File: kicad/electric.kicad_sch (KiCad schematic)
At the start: 11 parts, among them U1 NodeMCU1.0(ESP-12E), U2 LM7805_TO220

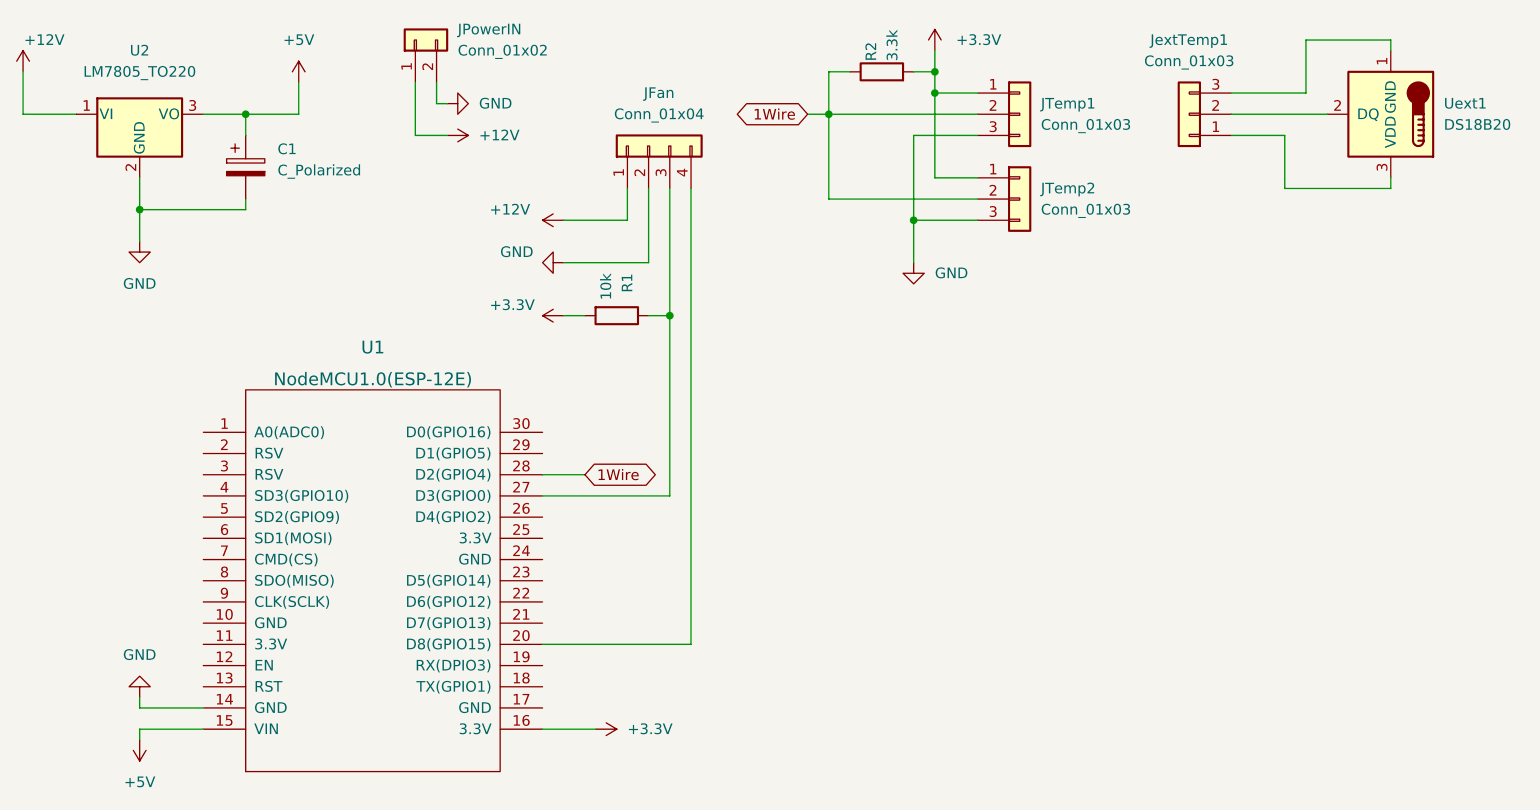
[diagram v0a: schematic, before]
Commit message: feat(kicad): added inverted pwm with npn transistor
Signed-off-by: Mario-F <github@fritschen.net>
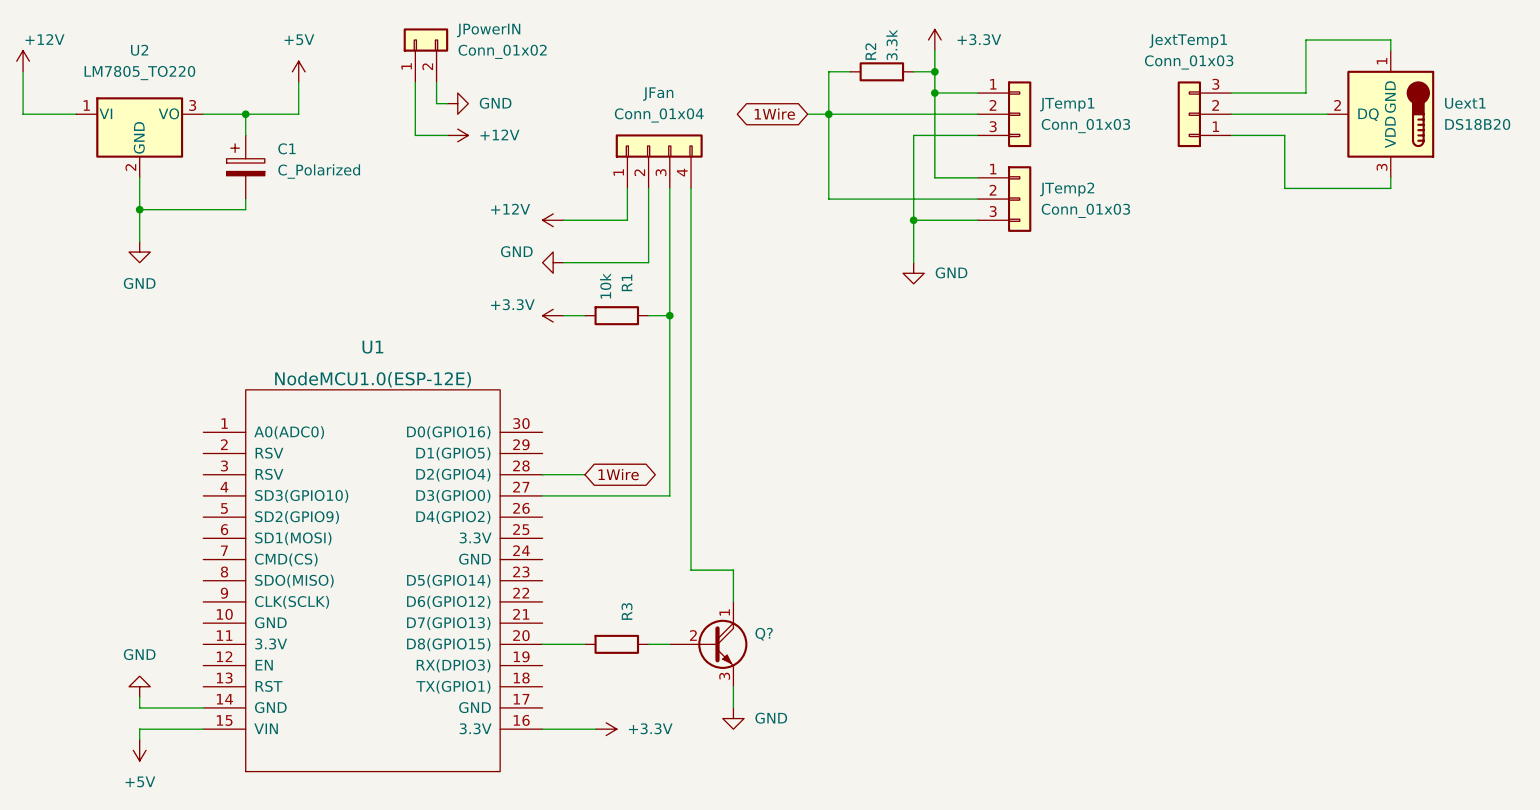
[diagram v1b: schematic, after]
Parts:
- added Q?: (no value), symbol Transistor_BJT:BC517
- added R3: (no value), symbol Device:R
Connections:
- net GND: now also Q?.3 (E)
- net at JFan.4 (Pin_4): now also Q?.1 (C); no longer U1.20 (D8(GPIO15))
- new net: Q?.2 (B), R3.1
- new net: R3.2, U1.20 (D8(GPIO15))
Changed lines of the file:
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@@
+    (stroke (width 0) (type default) (color 0 0 0 0))
+  )
+  (wire (pts (xy 102.87 80.01) (xy 102.87 83.82))
     (stroke (width 0) (type default) (color 0 0 0 0))
   )
@@
     (stroke (width 0) (type default) (color 0 0 0 0))
   )
+  (wire (pts (xy 102.87 93.98) (xy 102.87 96.52))
+    (stroke (width 0) (type default) (color 0 0 0 0))
+  )
   (wire (pts (xy 127 22.86) (xy 132.08 22.86))
     (stroke (width 0) (type default) (color 0 0 0 0))
@@
     (stroke (width 0) (type default) (color 0 0 0 0))
   )
+  (wire (pts (xy 97.79 34.29) (xy 97.79 80.01))
+    (stroke (width 0) (type default) (color 0 0 0 0))
+  )
   (wire (pts (xy 80.01 71.12) (xy 95.25 71.12))
     (stroke (width 0) (type default) (color 0 0 0 0))
@@
     (stroke (width 0) (type default) (color 0 0 0 0))
   )
+  (wire (pts (xy 92.71 88.9) (xy 95.25 88.9))
+    (stroke (width 0) (type default) (color 0 0 0 0))
+  )
   (wire (pts (xy 82.55 38.1) (xy 90.17 38.1))
     (stroke (width 0) (type default) (color 0 0 0 0))
   )
+  (wire (pts (xy 97.79 80.01) (xy 102.87 80.01))
+    (stroke (width 0) (type default) (color 0 0 0 0))
+  )
   (wire (pts (xy 132.08 35.56) (xy 114.3 35.56))
     (stroke (width 0) (type default) (color 0 0 0 0))
@@
     (stroke (width 0) (type default) (color 0 0 0 0))
   )
-  (wire (pts (xy 97.79 88.9) (xy 97.79 34.29))
-    (stroke (width 0) (type default) (color 0 0 0 0))
-  )
   (wire (pts (xy 114.3 20.32) (xy 114.3 25.4))
     (stroke (width 0) (type default) (color 0 0 0 0))
@@
     (stroke (width 0) (type default) (color 0 0 0 0))
   )
-  (wire (pts (xy 80.01 88.9) (xy 97.79 88.9))
+  (wire (pts (xy 80.01 88.9) (xy 85.09 88.9))
     (stroke (width 0) (type default) (color 0 0 0 0))
   )
@@
     )
     (pin "1")
+  )
+  (symbol (lib_id "Transistor_BJT:BC517") (at 100.33 88.9 0) (unit 1)
+    (in_bom yes) (on_board yes) (fields_autoplaced)
+    (property "Reference" "Q?" (id 0) (at 105.41 87.6299 0)
+      (effects (font (size 1.27 1.27)) (justify left))
+    )
+    (property "Value" "" (id 1) (at 105.41 90.1699 0)
+      (effects (font (size 1.27 1.27)) (justify left))
+    )
+    (property "Footprint" "" (id 2) (at 105.41 90.805 0)
+      (effects (font (size 1.27 1.27) italic) (justify left) hide)
+    )
+    (property "Datasheet" "https://www.onsemi.com/pub/Collateral/BC517-D74Z-D.PDF" (id 3) (at 100.33 88.9 0)
+      (effects (font (size 1.27 1.27)) (justify left) hide)
+    )
+    (pin "1")
+    (pin "2")
+    (pin "3")
   )
   (symbol (lib_id "power:+5V") (at 31.75 100.33 180) (unit 1)
@@
     (pin "3")
   )
+  (symbol (lib_id "power:GND") (at 102.87 96.52 0) (unit 1)
+    (in_bom yes) (on_board yes) (fields_autoplaced)
+    (property "Reference" "#PWR?" (id 0) (at 102.87 102.87 0)
+      (effects (font (size 1.27 1.27)) hide)
+    )
+    (property "Value" "GND" (id 1) (at 105.41 97.7899 0)
+      (effects (font (size 1.27 1.27)) (justify left))
+    )
+    (property "Footprint" "" (id 2) (at 102.87 96.52 0)
+      (effects (font (size 1.27 1.27)) hide)
+    )
+    (property "Datasheet" "" (id 3) (at 102.87 96.52 0)
+      (effects (font (size 1.27 1.27)) hide)
+    )
+    (pin "1")
+  )
   (symbol (lib_id "power:+3.3V") (at 86.36 99.06 270) (unit 1)
     (in_bom yes) (on_board yes) (fields_autoplaced)
@@
     )
     (pin "1")
+  )
+  (symbol (lib_id "Device:R") (at 88.9 88.9 270) (unit 1)
+    (in_bom yes) (on_board yes)
+    (property "Reference" "R3" (id 0) (at 90.17 83.82 0)
+      (effects (font (size 1.27 1.27)) (justify left))
+    )
+    (property "Value" "" (id 1) (at 87.63 83.82 0)
+      (effects (font (size 1.27 1.27)) (justify left))
+    )
+    (property "Footprint" "" (id 2) (at 88.9 87.122 90)
+      (effects (font (size 1.27 1.27)) hide)
+    )
+    (property "Datasheet" "~" (id 3) (at 88.9 88.9 0)
+      (effects (font (size 1.27 1.27)) hide)
+    )
+    (pin "1")
+    (pin "2")
   )
   (symbol (lib_id "Device:R") (at 120.65 20.32 90) (unit 1)
@@
       (reference "#PWR?") (unit 1) (value "GND") (footprint "")
     )
+    (path "/7943e171-c136-4b5f-8984-4dcdd0d9dc7a"
+      (reference "#PWR?") (unit 1) (value "GND") (footprint "")
+    )
     (path "/8770c33d-8988-4980-a1d7-71b8259e6385"
       (reference "#PWR?") (unit 1) (value "+3.3V") (footprint "")
@@
       (reference "JextTemp1") (unit 1) (value "Conn_01x03") (footprint "")
     )
+    (path "/328b655f-3682-4d72-b986-09747092cdfb"
+      (reference "Q?") (unit 1) (value "BC517") (footprint "Package_TO_SOT_THT:TO-92_Inline")
+    )
     (path "/43cd34eb-8147-4b4d-8f5f-1b40310c92b7"
       (reference "R1") (unit 1) (value "10k") (footprint "")
@@
       (reference "R2") (unit 1) (value "3.3k") (footprint "")
     )
+    (path "/dec3a3fc-aac1-4ba5-87a4-0f7cc72565ee"
+      (reference "R3") (unit 1) (value "3.3k") (footprint "")
+    )
     (path "/4244f2cf-53fb-48c6-88ac-de581a83aeb5"

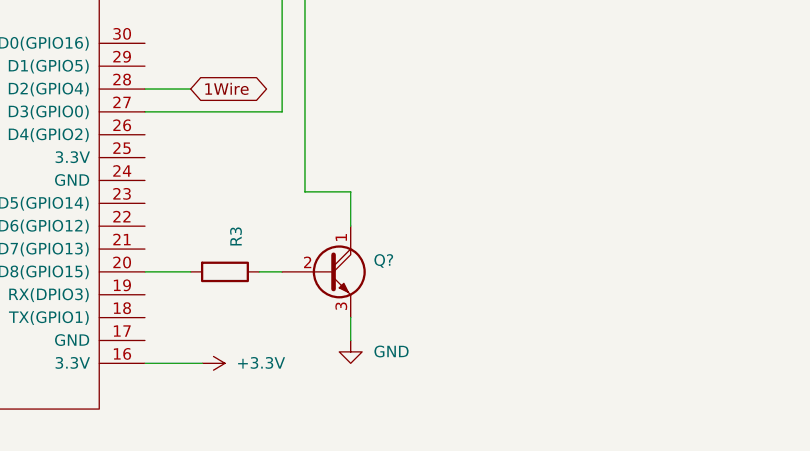
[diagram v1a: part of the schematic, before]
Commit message: perf(kicad): use 5k resistor for pwm drive
Signed-off-by: Mario-F <github@fritschen.net>
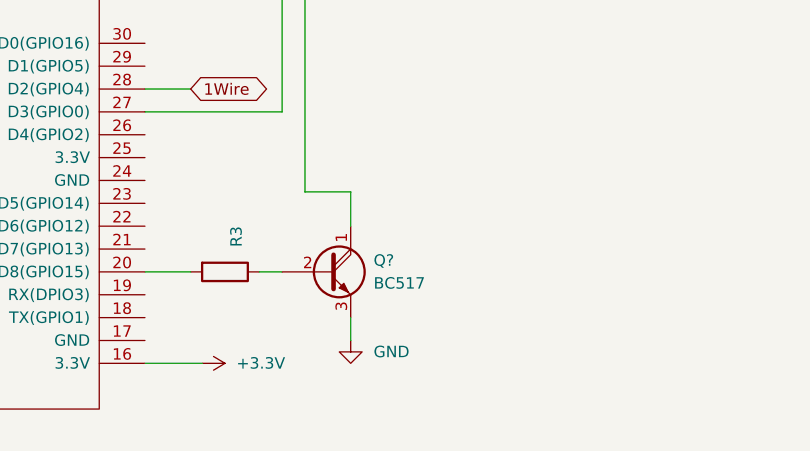
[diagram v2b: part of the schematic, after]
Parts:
- Q?: value (none) -> BC517; footprint (none) -> Package_TO_SOT_THT:TO-92_Inline
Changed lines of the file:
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@@
       (effects (font (size 1.27 1.27)) (justify left))
     )
-    (property "Value" "" (id 1) (at 105.41 90.1699 0)
-      (effects (font (size 1.27 1.27)) (justify left))
-    )
-    (property "Footprint" "" (id 2) (at 105.41 90.805 0)
+    (property "Value" "BC517" (id 1) (at 105.41 90.1699 0)
+      (effects (font (size 1.27 1.27)) (justify left))
+    )
+    (property "Footprint" "Package_TO_SOT_THT:TO-92_Inline" (id 2) (at 105.41 90.805 0)
       (effects (font (size 1.27 1.27) italic) (justify left) hide)
     )
@@
     )
     (path "/dec3a3fc-aac1-4ba5-87a4-0f7cc72565ee"
-      (reference "R3") (unit 1) (value "3.3k") (footprint "")
+      (reference "R3") (unit 1) (value "5k") (footprint "")
     )
     (path "/4244f2cf-53fb-48c6-88ac-de581a83aeb5"
